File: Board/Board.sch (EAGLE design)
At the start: 18 parts

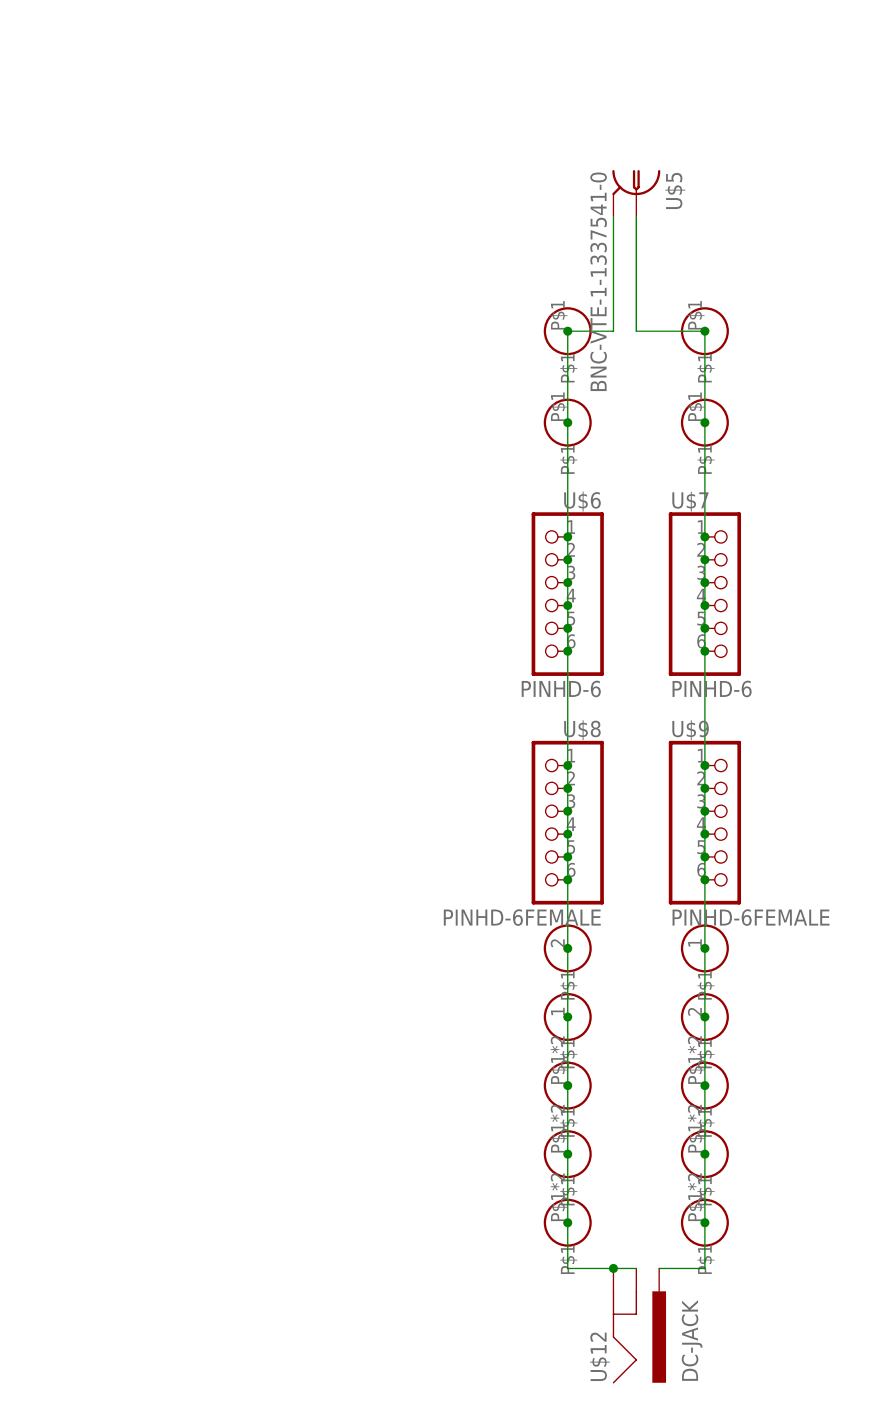
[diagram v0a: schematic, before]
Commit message: implemented various suggestions from the forum post
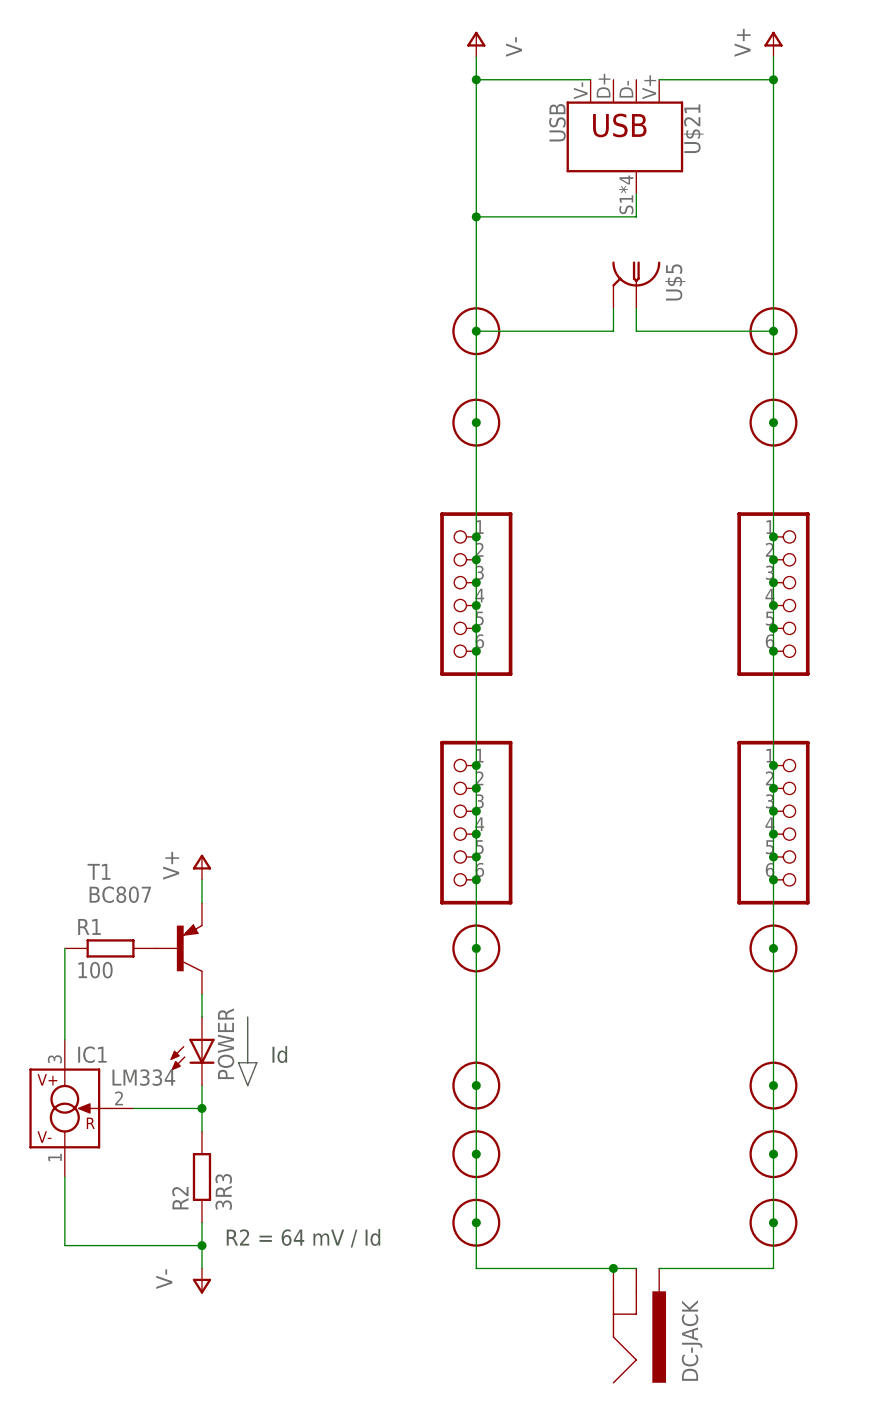
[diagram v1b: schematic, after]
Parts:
- removed U$11: TERMINAL-BLOCK-2PLUG-IN, AdapterBoard:TERMINAL-BLOCK-2PLUG-IN
- added IC1: LM334, linear:LM334SM
- added POWER: (no value), led:LED5MM
- added R1: 100, rcl:R-EU_R0603
- added R2: 3R3, rcl:R-EU_R0603
- added T1: BC807, transistor:BC807-16-PNP-SOT23-BEC
- added U$21: USB, AdapterBoard:USB
- U$1, U$3: value 6MM-BANANA-PLUG -> 6MM-BANANA-PLUGSCREW-BLACK; device AdapterBoard:6MM-BANANA-PLUG -> AdapterBoard:6MM-BANANA-PLUGSCREW-BLACK
- U$2, U$4: value 6MM-BANANA-PLUG -> 6MM-BANANA-PLUGSCREW-RED; device AdapterBoard:6MM-BANANA-PLUG -> AdapterBoard:6MM-BANANA-PLUGSCREW-RED
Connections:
- removed net +: U$10G$1.P$1, U$11G$2.P$1, U$12.PWR, U$15.P$1, U$16.P$1, U$19.P$1, U$2.P$1, U$4.P$1, U$5.C, U$7.1, U$7.2, U$7.3, U$7.4, U$7.5, U$7.6, U$9.1, U$9.2, U$9.3, U$9.4, U$9.5, U$9.6
- removed net -: U$1.P$1, U$10G$2.P$1, U$11G$1.P$1, U$12.GND, U$12.GNDBREAK, U$14.P$1, U$17.P$1, U$18.P$1, U$3.P$1, U$5.S, U$6.1, U$6.2, U$6.3, U$6.4, U$6.5, U$6.6, U$8.1, U$8.2, U$8.3, U$8.4, U$8.5, U$8.6
- new net N$1: IC1.R, POWER.C, R2.2
- new net N$2: R1.2, T1.B
- new net N$3: IC1.V+, R1.1
- new net N$4: POWER.A, T1.C
- new net V+: T1.E, U$10G$1.P$1, U$12.PWR, U$15.P$1, U$16.P$1, U$19.P$1, U$2.P$1, U$21.VBUS, U$4.P$1, U$5.C, U$7.1, U$7.2, U$7.3, U$7.4, U$7.5, U$7.6, U$9.1, U$9.2, U$9.3, U$9.4, U$9.5, U$9.6
- new net V-: IC1.V-, R2.1, U$1.P$1, U$10G$2.P$1, U$12.GND, U$12.GNDBREAK, U$14.P$1, U$17.P$1, U$18.P$1, U$21.GND, U$21.SHIELD, U$3.P$1, U$5.S, U$6.1, U$6.2, U$6.3, U$6.4, U$6.5, U$6.6, U$8.1, U$8.2, U$8.3, U$8.4, U$8.5, U$8.6
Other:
- note added: "Id"
- note added: "R2 = 64 mV / Id"
- moved on the sheet: U$5

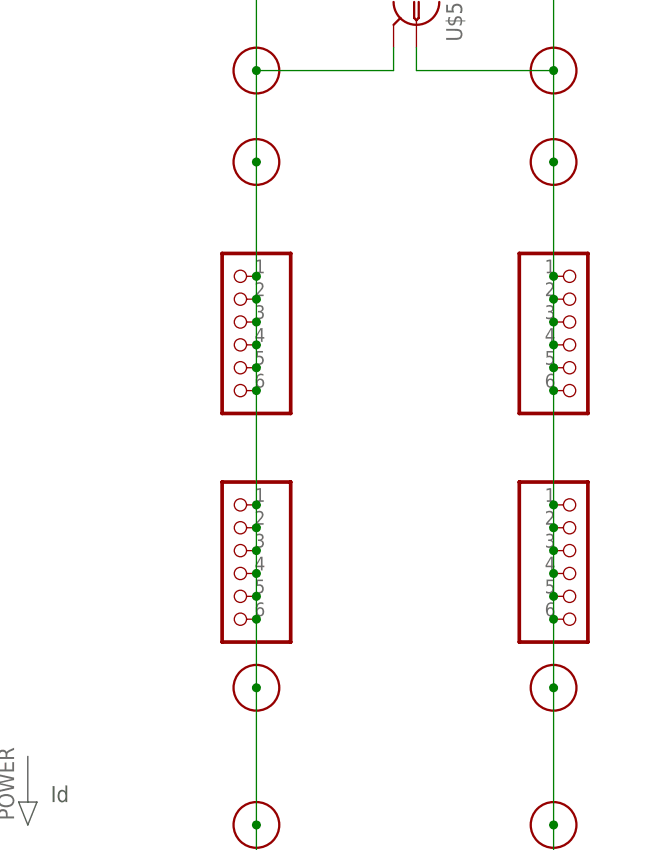
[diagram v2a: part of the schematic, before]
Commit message: updated BNC footprint
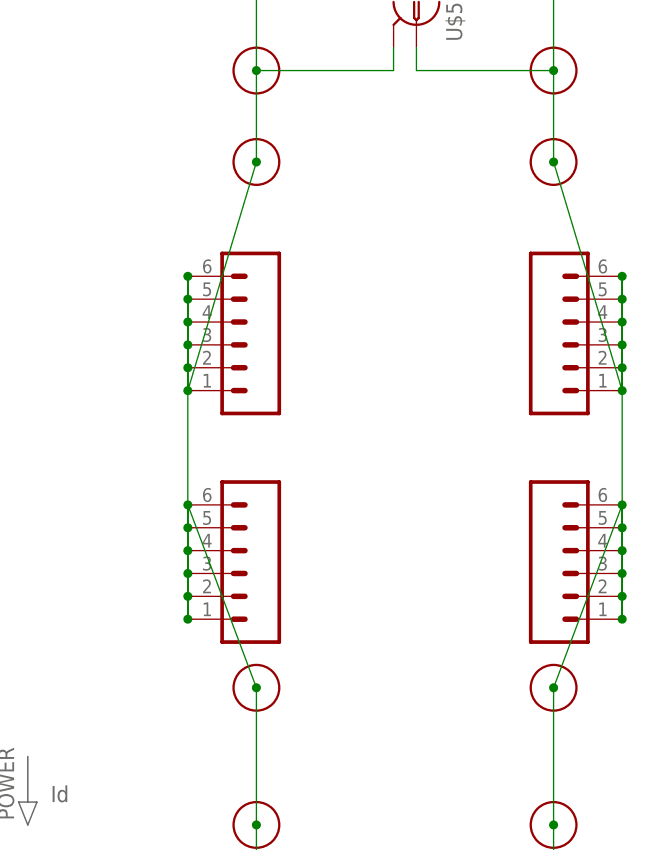
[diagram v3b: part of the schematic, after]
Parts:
- T1: device transistor:BC807-16-PNP-SOT23-BEC -> DC_LOAD_AU:-PNP-SOT23-BEC
- U$5: value BNC-VTE-1-1337541-0 -> BNC-V; device AdapterBoard:BNC-VTE-1-1337541-0 -> AdapterBoard:BNC-V
- U$6, U$7: value PINHD-6 -> (none); device AdapterBoard:PINHD-6 -> SparkFun-Connectors:CONN_06LOCK_LONGPADS
- U$8, U$9: value PINHD-6FEMALE -> (none); device AdapterBoard:PINHD-6FEMALE -> SparkFun-Connectors:CONN_06LOCK_LONGPADS

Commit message: updated pinheader 3d models
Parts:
- U$6, U$7: value (none) -> PINHEADER-1X6MALE_LOCK; device SparkFun-Connectors:CONN_06LOCK_LONGPADS -> AdapterBoard:PINHEADER-1X6MALE_LOCK
- U$8, U$9: value (none) -> PINHEADER-1X6FEMALE_LOCK; device SparkFun-Connectors:CONN_06LOCK_LONGPADS -> AdapterBoard:PINHEADER-1X6FEMALE_LOCK
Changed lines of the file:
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@@
 <part name="U$4" library="AdapterBoard" library_urn="urn:adsk.eagle:library:6658125" deviceset="6MM-BANANA-PLUG" device="SCREW-RED" package3d_urn="urn:adsk.eagle:package:6717381/2" value="6MM-BANANA-PLUGSCREW-RED"/>
 <part name="U$5" library="AdapterBoard" library_urn="urn:adsk.eagle:library:6658125" deviceset="BNC-V" device="" package3d_urn="urn:adsk.eagle:package:7174046/2" value="BNC-V"/>
-<part name="U$6" library="SparkFun-Connectors" library_urn="urn:adsk.eagle:library:513" deviceset="CONN_06" device="LOCK_LONGPADS" package3d_urn="urn:adsk.eagle:package:38121/1"/>
-<part name="U$7" library="SparkFun-Connectors" library_urn="urn:adsk.eagle:library:513" deviceset="CONN_06" device="LOCK_LONGPADS" package3d_urn="urn:adsk.eagle:package:38121/1"/>
-<part name="U$8" library="SparkFun-Connectors" library_urn="urn:adsk.eagle:library:513" deviceset="CONN_06" device="LOCK_LONGPADS" package3d_urn="urn:adsk.eagle:package:38121/1"/>
-<part name="U$9" library="SparkFun-Connectors" library_urn="urn:adsk.eagle:library:513" deviceset="CONN_06" device="LOCK_LONGPADS" package3d_urn="urn:adsk.eagle:package:38121/1"/>
+<part name="U$6" library="AdapterBoard" library_urn="urn:adsk.eagle:library:6658125" deviceset="PINHEADER-1X6" device="MALE_LOCK" package3d_urn="urn:adsk.eagle:package:7198025/2"/>
+<part name="U$7" library="AdapterBoard" library_urn="urn:adsk.eagle:library:6658125" deviceset="PINHEADER-1X6" device="MALE_LOCK" package3d_urn="urn:adsk.eagle:package:7198025/2"/>
+<part name="U$8" library="AdapterBoard" library_urn="urn:adsk.eagle:library:6658125" deviceset="PINHEADER-1X6" device="FEMALE_LOCK" package3d_urn="urn:adsk.eagle:package:7198026/2"/>
+<part name="U$9" library="AdapterBoard" library_urn="urn:adsk.eagle:library:6658125" deviceset="PINHEADER-1X6" device="FEMALE_LOCK" package3d_urn="urn:adsk.eagle:package:7198026/2"/>
 <part name="U$10" library="AdapterBoard" library_urn="urn:adsk.eagle:library:6658125" deviceset="TERMINAL-BLOCK-2" device="" package3d_urn="urn:adsk.eagle:package:6658197/4"/>
 <part name="U$12" library="Parts" library_urn="urn:adsk.eagle:library:2304016" deviceset="DC-JACK" device="" package3d_urn="urn:adsk.eagle:package:2338719/2"/>

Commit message: increased constant current feedback resistor
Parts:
- R2: value 3R3 -> 36
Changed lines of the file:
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@@
 <part name="T1" library="DC_LOAD_AU" library_urn="urn:adsk.eagle:library:220454" deviceset="*-PNP-" device="SOT23-BEC" package3d_urn="urn:adsk.eagle:package:220536/2" value="BC807"/>
 <part name="R1" library="rcl" library_urn="urn:adsk.eagle:library:334" deviceset="R-EU_" device="R0603" package3d_urn="urn:adsk.eagle:package:23555/2" value="100"/>
-<part name="R2" library="rcl" library_urn="urn:adsk.eagle:library:334" deviceset="R-EU_" device="R0603" package3d_urn="urn:adsk.eagle:package:23555/2" value="3R3"/>
+<part name="R2" library="rcl" library_urn="urn:adsk.eagle:library:334" deviceset="R-EU_" device="R0603" package3d_urn="urn:adsk.eagle:package:23555/2" value="36"/>
 <part name="P+1" library="supply1" library_urn="urn:adsk.eagle:library:371" deviceset="V+" device=""/>
 <part name="P-1" library="supply1" library_urn="urn:adsk.eagle:library:371" deviceset="V-" device=""/>

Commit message: reverted to old bnc footprint
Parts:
- U$5: value BNC-V -> BNC-VTE-1-1337541-0; device AdapterBoard:BNC-V -> AdapterBoard:BNC-VTE-1-1337541-0
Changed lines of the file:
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@@
 <part name="U$3" library="AdapterBoard" library_urn="urn:adsk.eagle:library:6658125" deviceset="6MM-BANANA-PLUG" device="SCREW-BLACK" package3d_urn="urn:adsk.eagle:package:6717096/2" value="6MM-BANANA-PLUGSCREW-BLACK"/>
 <part name="U$4" library="AdapterBoard" library_urn="urn:adsk.eagle:library:6658125" deviceset="6MM-BANANA-PLUG" device="SCREW-RED" package3d_urn="urn:adsk.eagle:package:6717381/2" value="6MM-BANANA-PLUGSCREW-RED"/>
-<part name="U$5" library="AdapterBoard" library_urn="urn:adsk.eagle:library:6658125" deviceset="BNC-V" device="" package3d_urn="urn:adsk.eagle:package:7174046/2" value="BNC-V"/>
+<part name="U$5" library="AdapterBoard" library_urn="urn:adsk.eagle:library:6658125" deviceset="BNC-V" device="TE-1-1337541-0" package3d_urn="urn:adsk.eagle:package:6658128/5" value="BNC-VTE-1-1337541-0"/>
 <part name="U$6" library="AdapterBoard" library_urn="urn:adsk.eagle:library:6658125" deviceset="PINHEADER-1X6" device="MALE_LOCK" package3d_urn="urn:adsk.eagle:package:7198025/2"/>
 <part name="U$7" library="AdapterBoard" library_urn="urn:adsk.eagle:library:6658125" deviceset="PINHEADER-1X6" device="MALE_LOCK" package3d_urn="urn:adsk.eagle:package:7198025/2"/>

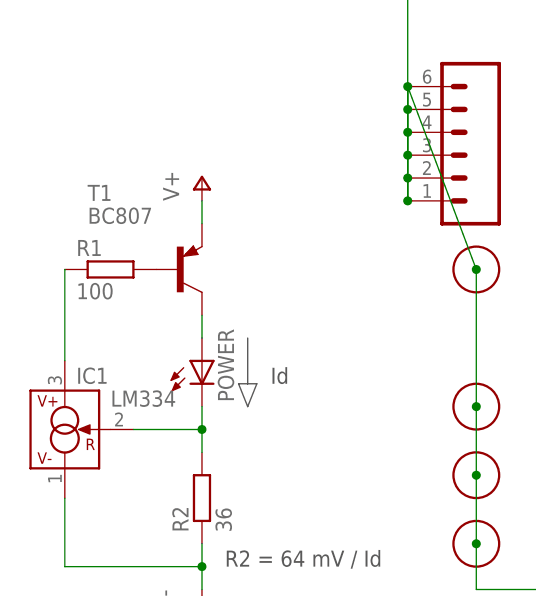
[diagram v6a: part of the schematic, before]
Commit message: updated constant current source for power LED
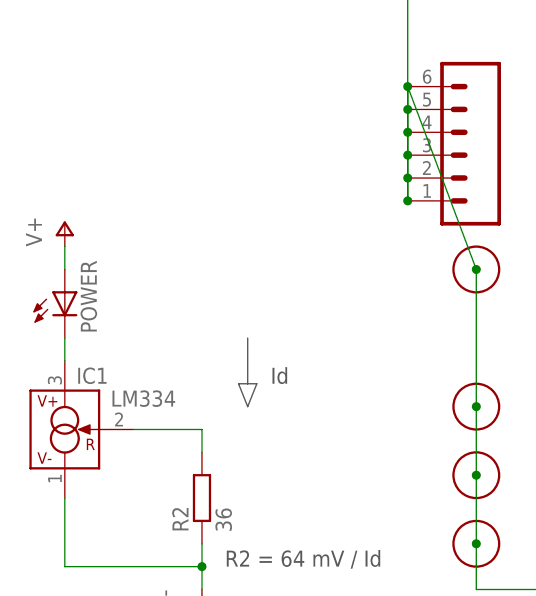
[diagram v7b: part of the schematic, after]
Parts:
- removed R1: 100, rcl:R-EU_R0603
- removed T1: BC807, DC_LOAD_AU:-PNP-SOT23-BEC
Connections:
- removed net N$3: IC1.V+, R1.1
- removed net N$4: POWER.A, T1.C
- net N$1: no longer POWER.C
- net N$2: now also IC1.V+, POWER.C; no longer R1.2, T1.B
- net V+: now also POWER.A; no longer T1.E
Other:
- moved on the sheet: POWER
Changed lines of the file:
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@@
 <part name="IC1" library="linear" library_urn="urn:adsk.eagle:library:262" deviceset="LM*34" device="SM" package3d_urn="urn:adsk.eagle:package:16404/2" technology="3" value="LM334"/>
 <part name="POWER" library="led" library_urn="urn:adsk.eagle:library:259" deviceset="LED" device="5MM" package3d_urn="urn:adsk.eagle:package:15799/2"/>
-<part name="T1" library="DC_LOAD_AU" library_urn="urn:adsk.eagle:library:220454" deviceset="*-PNP-" device="SOT23-BEC" package3d_urn="urn:adsk.eagle:package:220536/2" value="BC807"/>
-<part name="R1" library="rcl" library_urn="urn:adsk.eagle:library:334" deviceset="R-EU_" device="R0603" package3d_urn="urn:adsk.eagle:package:23555/2" value="100"/>
 <part name="R2" library="rcl" library_urn="urn:adsk.eagle:library:334" deviceset="R-EU_" device="R0603" package3d_urn="urn:adsk.eagle:package:23555/2" value="36"/>
 <part name="P+1" library="supply1" library_urn="urn:adsk.eagle:library:371" deviceset="V+" device=""/>
@@
 <attribute name="VALUE" x="-33.02" y="-20.32" size="1.778" layer="96"/>
 </instance>
-<instance part="POWER" gate="G$1" x="-22.86" y="-15.24" smashed="yes">
-<attribute name="NAME" x="-19.304" y="-19.812" size="1.778" layer="95" rot="R90"/>
-<attribute name="VALUE" x="-17.145" y="-19.812" size="1.778" layer="96" rot="R90"/>
-</instance>
-<instance part="T1" gate="G$1" x="-25.4" y="-5.08" smashed="yes">
-<attribute name="NAME" x="-35.56" y="2.54" size="1.778" layer="95"/>
-<attribute name="VALUE" x="-35.56" y="0" size="1.778" layer="96"/>
-</instance>
-<instance part="R1" gate="G$1" x="-33.02" y="-5.08" smashed="yes">
-<attribute name="NAME" x="-36.83" y="-3.5814" size="1.778" layer="95"/>
-<attribute name="VALUE" x="-36.83" y="-8.382" size="1.778" layer="96"/>
+<instance part="POWER" gate="G$1" x="-38.1" y="-7.62" smashed="yes">
+<attribute name="NAME" x="-34.544" y="-12.192" size="1.778" layer="95" rot="R90"/>
+<attribute name="VALUE" x="-32.385" y="-12.192" size="1.778" layer="96" rot="R90"/>
 </instance>
 <instance part="R2" gate="G$1" x="-22.86" y="-30.48" smashed="yes" rot="R90">
@@
 <attribute name="VALUE" x="-27.94" y="-40.64" size="1.778" layer="96" rot="R270"/>
 </instance>
-<instance part="P+2" gate="1" x="-22.86" y="5.08" smashed="yes">
-<attribute name="VALUE" x="-25.4" y="2.54" size="1.778" layer="96" rot="R90"/>
+<instance part="P+2" gate="1" x="-38.1" y="0" smashed="yes">
+<attribute name="VALUE" x="-40.64" y="-2.54" size="1.778" layer="96" rot="R90"/>
 </instance>
 <instance part="U$21" gate="G$1" x="22.86" y="83.82" smashed="yes" rot="R270">
@@
 </busses>
 <nets>
-<net name="N$2" class="0">
-<segment>
-<pinref part="T1" gate="G$1" pin="B"/>
-<pinref part="R1" gate="G$1" pin="2"/>
-</segment>
-</net>
-<net name="N$3" class="0">
-<segment>
-<pinref part="R1" gate="G$1" pin="1"/>
-<pinref part="IC1" gate="G$1" pin="V+"/>
-<wire x1="-38.1" y1="-5.08" x2="-38.1" y2="-15.24" width="0.1524" layer="91"/>
-</segment>
-</net>
 <net name="N$1" class="0">
 <segment>
 <pinref part="R2" gate="G$1" pin="2"/>
-<pinref part="POWER" gate="G$1" pin="C"/>
-<wire x1="-22.86" y1="-20.32" x2="-22.86" y2="-22.86" width="0.1524" layer="91"/>
 <pinref part="IC1" gate="G$1" pin="R"/>
 <wire x1="-22.86" y1="-22.86" x2="-22.86" y2="-25.4" width="0.1524" layer="91"/>
 <wire x1="-30.48" y1="-22.86" x2="-22.86" y2="-22.86" width="0.1524" layer="91"/>
-<junction x="-22.86" y="-22.86"/>
-</segment>
-</net>
-<net name="N$4" class="0">
-<segment>
-<pinref part="T1" gate="G$1" pin="C"/>
-<pinref part="POWER" gate="G$1" pin="A"/>
-<wire x1="-22.86" y1="-10.16" x2="-22.86" y2="-12.7" width="0.1524" layer="91"/>
 </segment>
 </net>
@@
 </segment>
 <segment>
+<pinref part="POWER" gate="G$1" pin="A"/>
 <pinref part="P+2" gate="1" pin="V+"/>
-<pinref part="T1" gate="G$1" pin="E"/>
-<wire x1="-22.86" y1="2.54" x2="-22.86" y2="0" width="0.1524" layer="91"/>
+<wire x1="-38.1" y1="-2.54" x2="-38.1" y2="-5.08" width="0.1524" layer="91"/>
 </segment>
 </net>
@@
 </segment>
 </net>
+<net name="N$2" class="0">
+<segment>
+<pinref part="IC1" gate="G$1" pin="V+"/>
+<pinref part="POWER" gate="G$1" pin="C"/>
+<wire x1="-38.1" y1="-12.7" x2="-38.1" y2="-15.24" width="0.1524" layer="91"/>
+</segment>
+</net>
